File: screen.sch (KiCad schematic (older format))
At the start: 2 parts

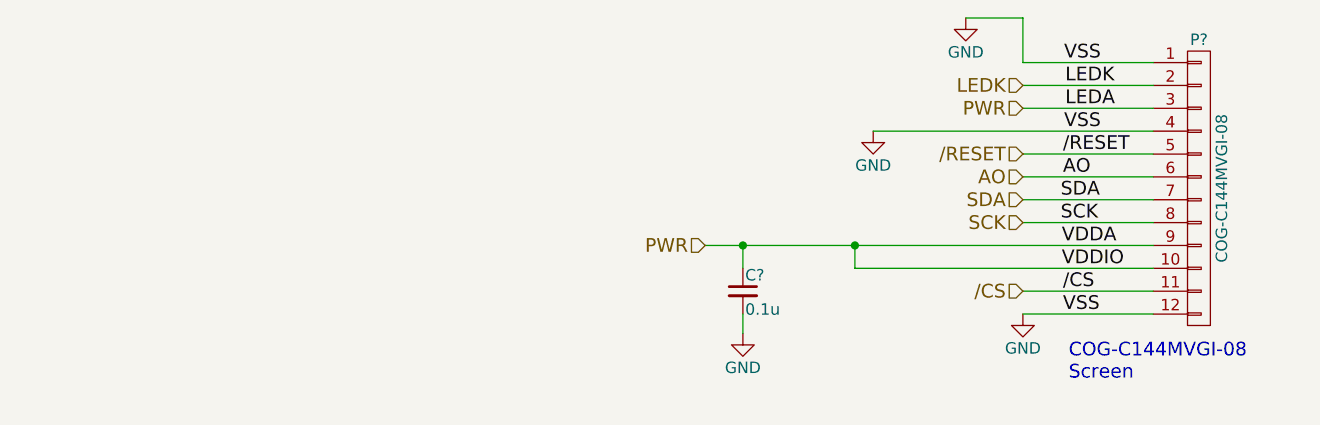
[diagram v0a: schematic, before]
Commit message: moved power circuits to separate sheet and used Vusb label for input to buck converter
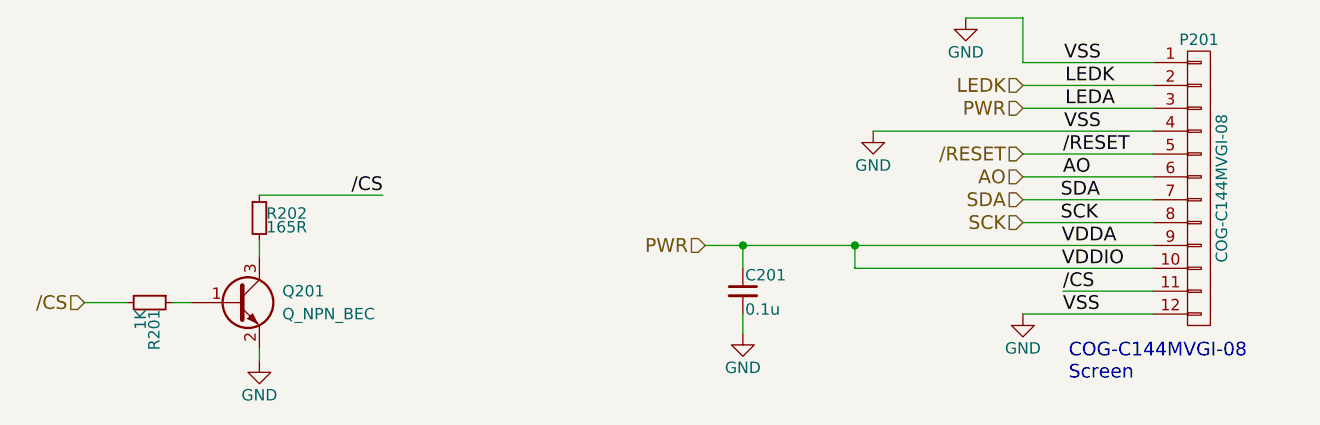
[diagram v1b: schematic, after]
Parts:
- added Q201: Q_NPN_BEC, symbol Q_NPN_BEC
- added R201: 1K, symbol R_Small
- added R202: 165R, symbol R_Small
- gave numbers to parts that had none: 2
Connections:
- net /CS: now also R201.2, R202.1
- net GND: now also Q201.2 (E)
- new net: Q201.1 (B), R201.1
- new net: Q201.3 (C), R202.2
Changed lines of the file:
@@
 $Descr A4 11693 8268
 encoding utf-8
-Sheet 2 2
+Sheet 2 3
 Title ""
 Date ""
@@
 Wire Wire Line
 	7175 3200 8480 3200
-Wire Wire Line
-	8480 3300 7910 3300
 Wire Wire Line
 	8480 3400 7910 3400
@@
 VSS
 $Comp
-L GND #PWR?
+L GND #PWR204
 U 1 1 591A1FEF
 P 7660 2105
-F 0 "#PWR?" H 7660 1855 50  0001 C CNN
+F 0 "#PWR204" H 7660 1855 50  0001 C CNN
 F 1 "GND" H 7660 1955 50  0000 C CNN
 F 2 "" H 7660 2105 50  0000 C CNN
@@
 	7910 2105 7660 2105
 $Comp
-L GND #PWR?
+L GND #PWR205
 U 1 1 591A2013
 P 7910 3400
-F 0 "#PWR?" H 7910 3150 50  0001 C CNN
+F 0 "#PWR205" H 7910 3150 50  0001 C CNN
 F 1 "GND" H 7910 3250 50  0000 C CNN
 F 2 "" H 7910 3400 50  0000 C CNN
@@
 Connection ~ 7175 3100
 $Comp
-L C_Small C?
+L C_Small C201
 U 1 1 591A2063
 P 6685 3300
-F 0 "C?" H 6695 3370 50  0000 L CNN
+F 0 "C201" H 6695 3370 50  0000 L CNN
 F 1 "0.1u" H 6695 3220 50  0000 L CNN
 F 2 "" H 6685 3300 50  0000 C CNN
@@
 Connection ~ 6685 3100
 $Comp
-L GND #PWR?
+L GND #PWR202
 U 1 1 591A2149
 P 6685 3485
-F 0 "#PWR?" H 6685 3235 50  0001 C CNN
+F 0 "#PWR202" H 6685 3235 50  0001 C CNN
 F 1 "GND" H 6685 3335 50  0000 C CNN
 F 2 "" H 6685 3485 50  0000 C CNN
@@
 Wire Wire Line
 	6685 3400 6685 3485
-Text HLabel 7910 3300 0    60   Input ~ 0
+Text HLabel 3805 3350 0    60   Input ~ 0
 /CS
 Text HLabel 7910 3000 0    60   Input ~ 0
@@
 LEDK
 $Comp
-L GND #PWR?
+L GND #PWR203
 U 1 1 591A2227
 P 7255 2600
-F 0 "#PWR?" H 7255 2350 50  0001 C CNN
+F 0 "#PWR203" H 7255 2350 50  0001 C CNN
 F 1 "GND" H 7255 2450 50  0000 C CNN
 F 2 "" H 7255 2600 50  0000 C CNN
@@
 COG-C144MVGI-08\nScreen
 $Comp
-L COG-C144MVGI-08 P?
+L COG-C144MVGI-08 P201
 U 1 1 591CA42C
 P 8680 2850
-F 0 "P?" H 8680 3500 50  0000 C CNN
+F 0 "P201" H 8680 3500 50  0000 C CNN
 F 1 "COG-C144MVGI-08" V 8780 2850 50  0000 C CNN
 F 2 "" H 8680 2850 50  0000 C CNN
@@
 	1    0    0    -1
 $EndComp
+$Comp
+L Q_NPN_BEC Q201
+U 1 1 592BA7C0
+P 4470 3350
+F 0 "Q201" H 4670 3400 50  0000 L CNN
+F 1 "Q_NPN_BEC" H 4670 3300 50  0000 L CNN
+F 2 "" H 4670 3450 50  0000 C CNN
+F 3 "" H 4470 3350 50  0000 C CNN
+	1    4470 3350
+	1    0    0    -1
+$EndComp
+$Comp
+L R_Small R202
+U 1 1 592BA800
+P 4570 2980
+F 0 "R202" H 4600 3000 50  0000 L CNN
+F 1 "165R" H 4600 2940 50  0000 L CNN
+F 2 "" H 4570 2980 50  0000 C CNN
+F 3 "" H 4570 2980 50  0000 C CNN
+F 4 "Value" H 4570 2980 60  0001 C CNN "Fieldname"
+	1    4570 2980
+	1    0    0    -1
+$EndComp
+Wire Wire Line
+	4570 3080 4570 3150
+$Comp
+L R_Small R201
+U 1 1 592BA8D3
+P 4090 3350
+F 0 "R201" H 4120 3370 50  0000 L CNN
+F 1 "1K" H 4120 3310 50  0000 L CNN
+F 2 "" H 4090 3350 50  0000 C CNN
+F 3 "" H 4090 3350 50  0000 C CNN
+F 4 "Value" H 4090 3350 60  0001 C CNN "Fieldname"
+	1    4090 3350
+	0    1    1    0
+$EndComp
+Wire Wire Line
+	4270 3350 4190 3350
+$Comp
+L GND #PWR201
+U 1 1 592BA9AE
+P 4570 3605
+F 0 "#PWR201" H 4570 3355 50  0001 C CNN
+F 1 "GND" H 4570 3455 50  0000 C CNN
+F 2 "" H 4570 3605 50  0000 C CNN
+F 3 "" H 4570 3605 50  0000 C CNN
+	1    4570 3605
+	1    0    0    -1
+$EndComp
+Wire Wire Line
+	4570 3550 4570 3605
+Wire Wire Line
+	3990 3350 3805 3350
+Wire Wire Line
+	4570 2880 5110 2880
+Text Label 5110 2880 2    60   ~ 0
+/CS
+Wire Wire Line
+	8480 3300 8085 3300
 $EndSCHEMATC
